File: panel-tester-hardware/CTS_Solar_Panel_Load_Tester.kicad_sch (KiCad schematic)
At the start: 11 parts, among them J1 Screw_Terminal_01x02, J2 Conn_01x02_Pin, J3 Conn_01x07, U1 INA219AxD, U2 LM311PW

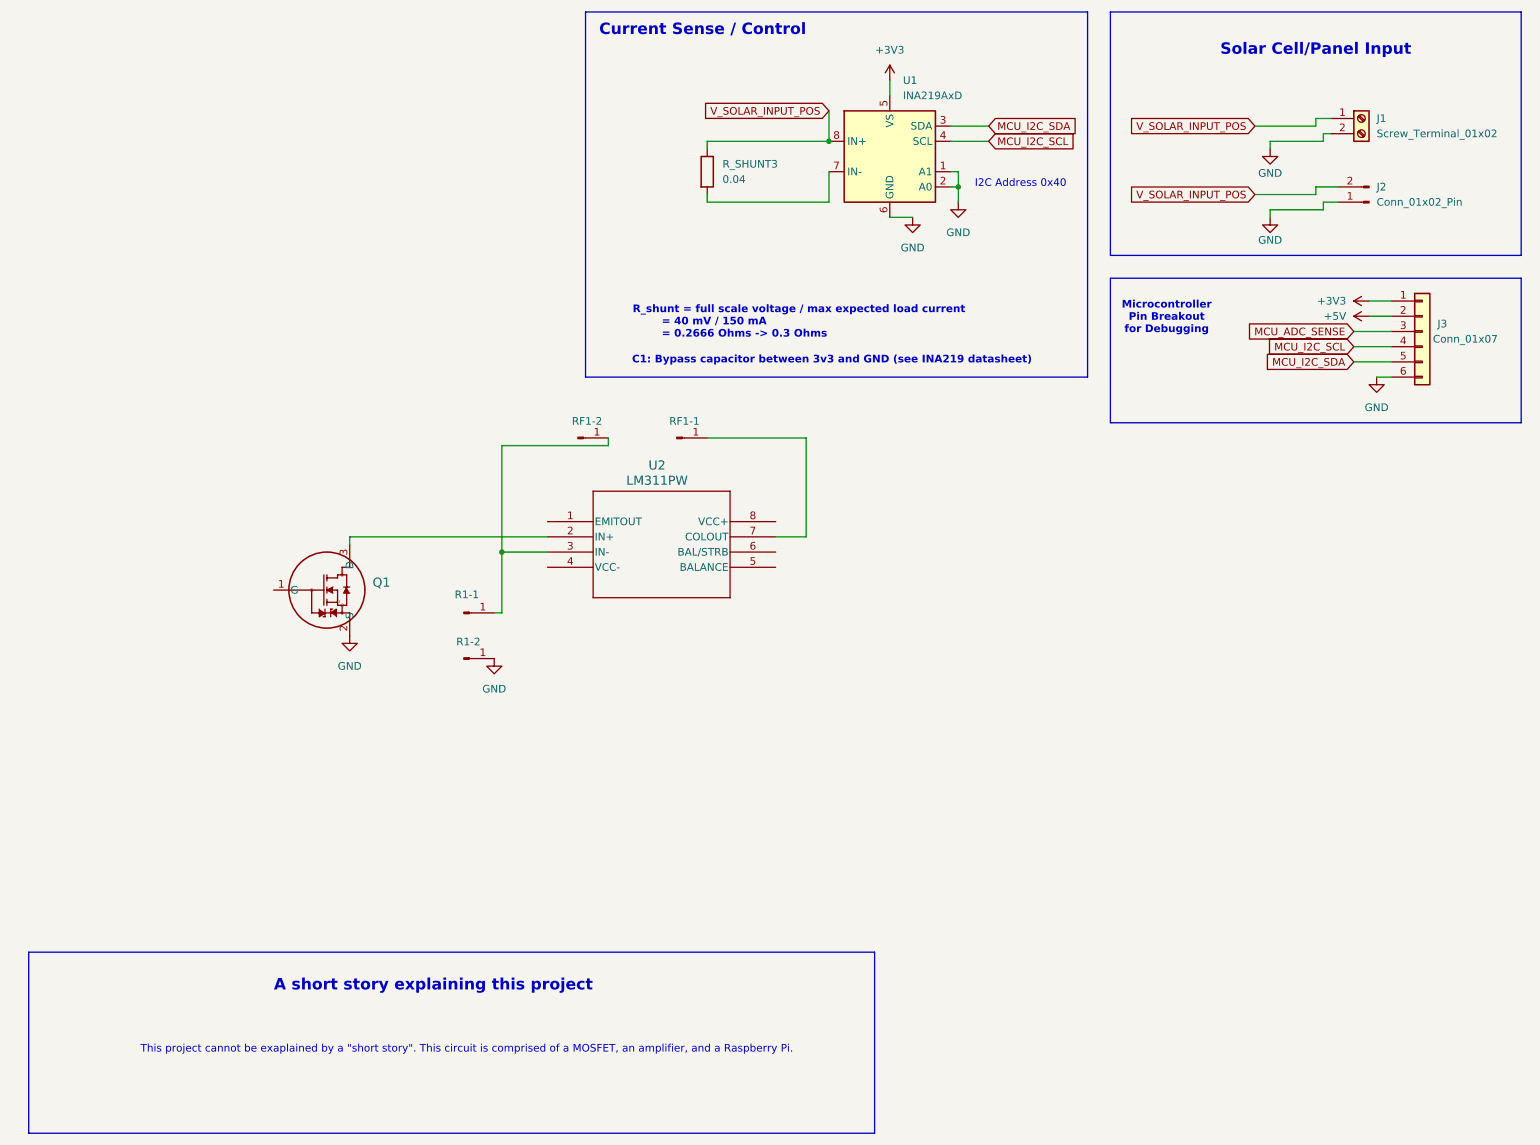
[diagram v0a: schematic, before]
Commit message: fixed footprints and added headers
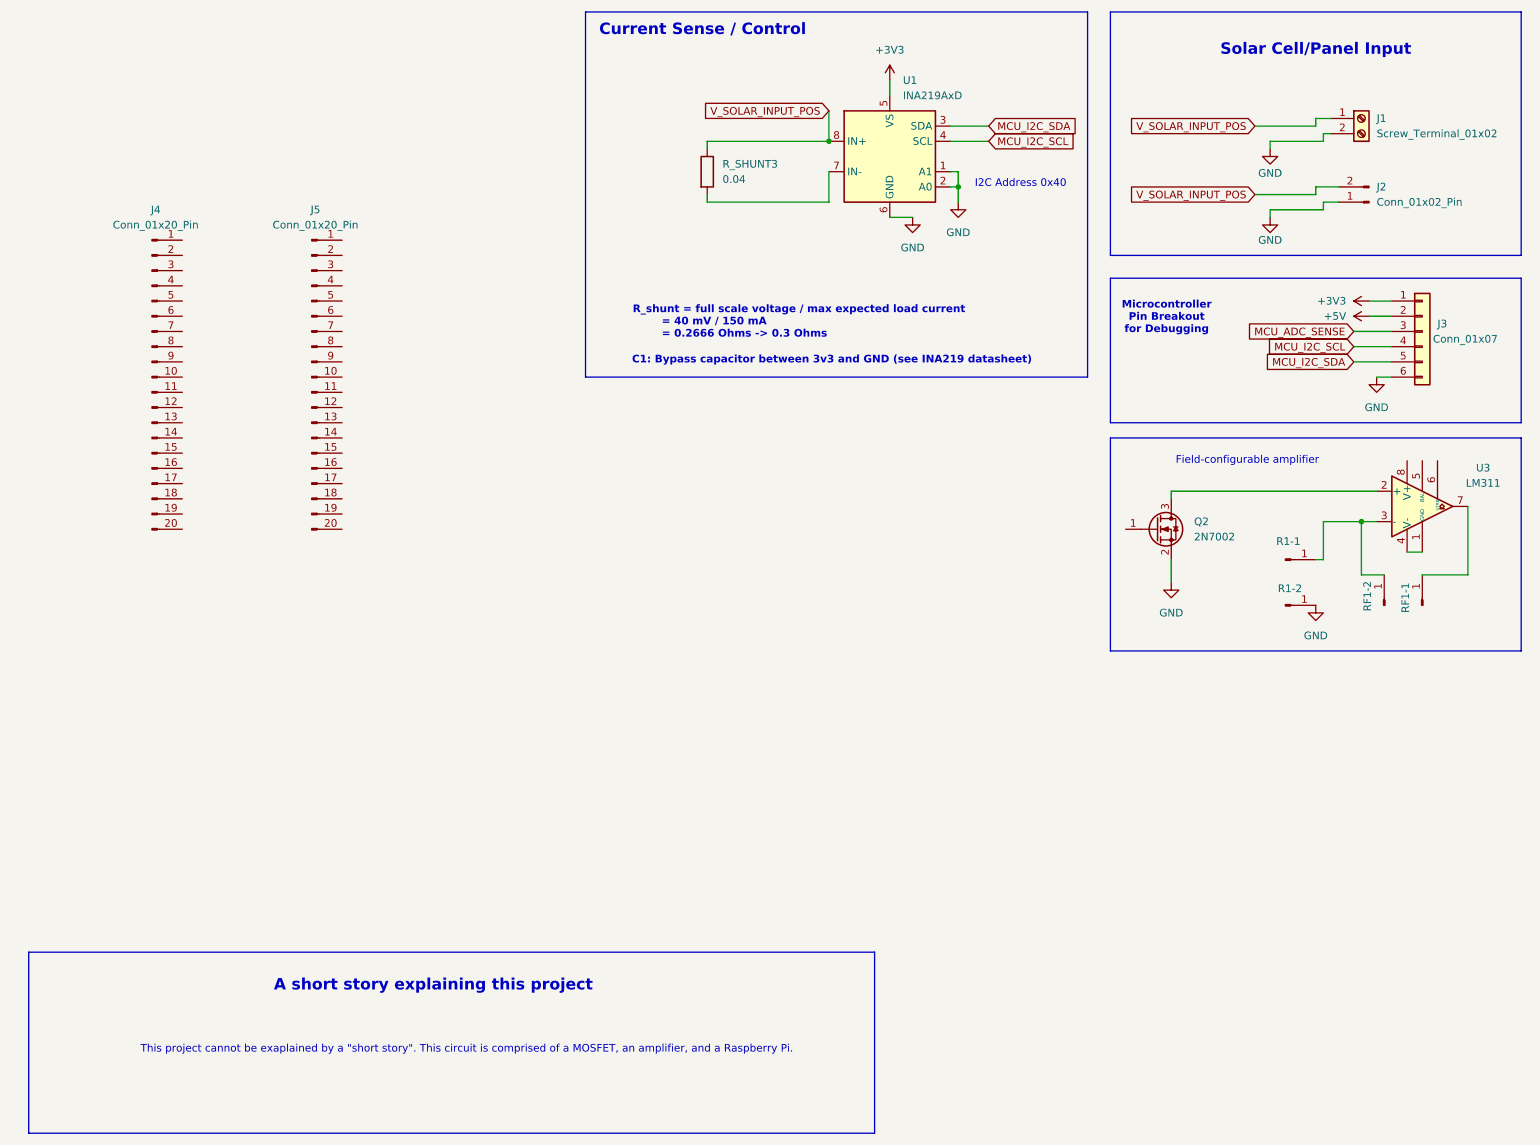
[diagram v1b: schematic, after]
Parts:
- removed Q1: ~, mosfet:TO-236AB_SOT23_NEX, symbol mosfet:2N7002NXAKR
- removed U2: LM311PW, PW8, symbol lm311opamp:LM311PW
- added J4, J5: Conn_01x20_Pin, Connector_PinHeader_2.54mm:PinHeader_1x20_P2.54mm_Vertical, symbol Connector:Conn_01x20_Pin
- added Q2: 2N7002, Package_TO_SOT_SMD:SOT-23, symbol Transistor_FET:2N7002
- added U3: LM311, Package_SO:SOIC-8-1EP_3.9x4.9mm_P1.27mm_EP2.95x4.9mm_Mask2.71x3.4mm, symbol Comparator:LM311
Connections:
- net GND: now also Q2.2 (S)
- net at R1-1.1 (Pin_1), RF1-2.1 (Pin_1): now also U3.3 (-)
- net at RF1-1.1 (Pin_1): now also U3.7
- new net: Q2.3 (D), U3.2 (+)
- new net: U3.1 (GND), U3.4 (V-)
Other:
- note added: "Field-configurable amplifier"
- moved on the sheet: R1-1, R1-2, RF1-1, RF1-2

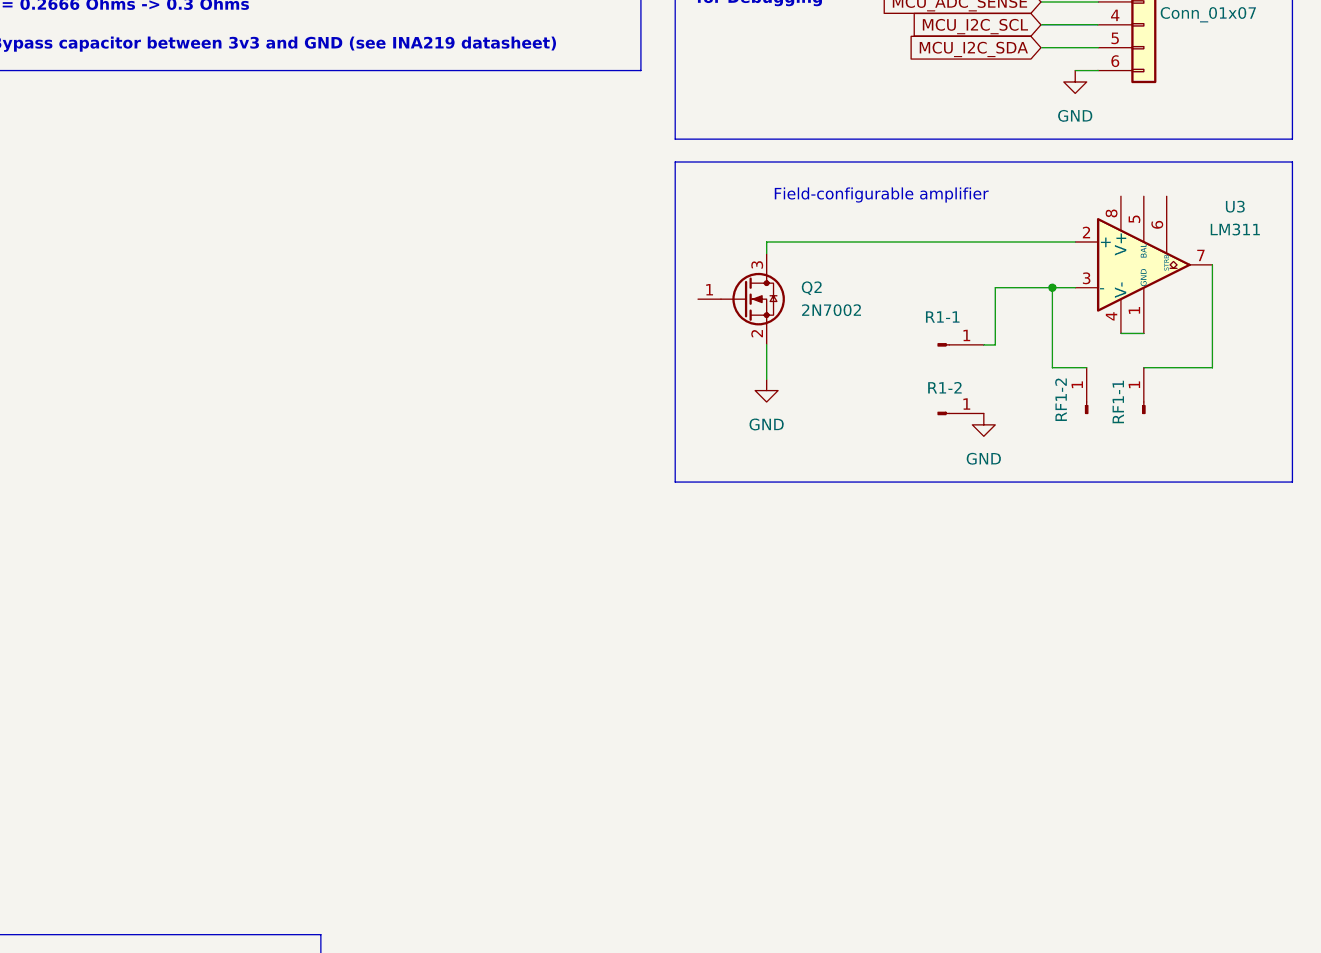
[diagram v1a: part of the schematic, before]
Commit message: added DAC
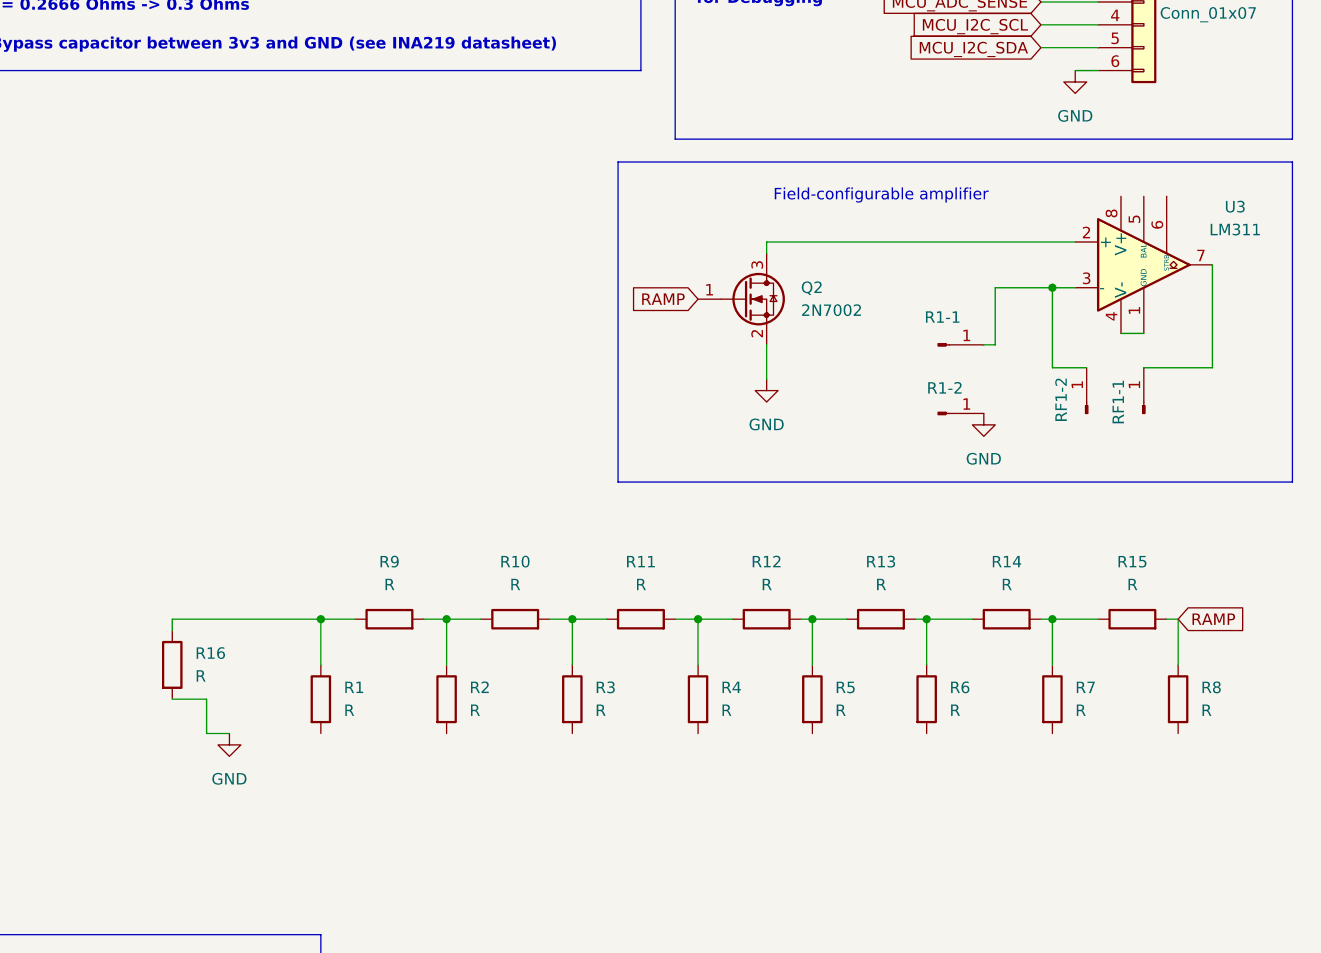
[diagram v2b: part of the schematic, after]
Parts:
- added R1, R10, R11, R12, R13, R14, R15, R16, R2, R3, R4, R5, R6, R7, R8, R9: R, symbol Device:R
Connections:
- net GND: now also R16.2
- net RAMP: now reaches Q2.1 (G)
- net RAMP: now also R15.2, R8.1
- new net: R13.2, R14.1, R6.1
- new net: R14.2, R15.1, R7.1
- new net: R10.2, R11.1, R3.1
- new net: R10.1, R2.1, R9.2
- new net: R1.1, R16.1, R9.1
- new net: R12.2, R13.1, R5.1
- new net: R11.2, R12.1, R4.1

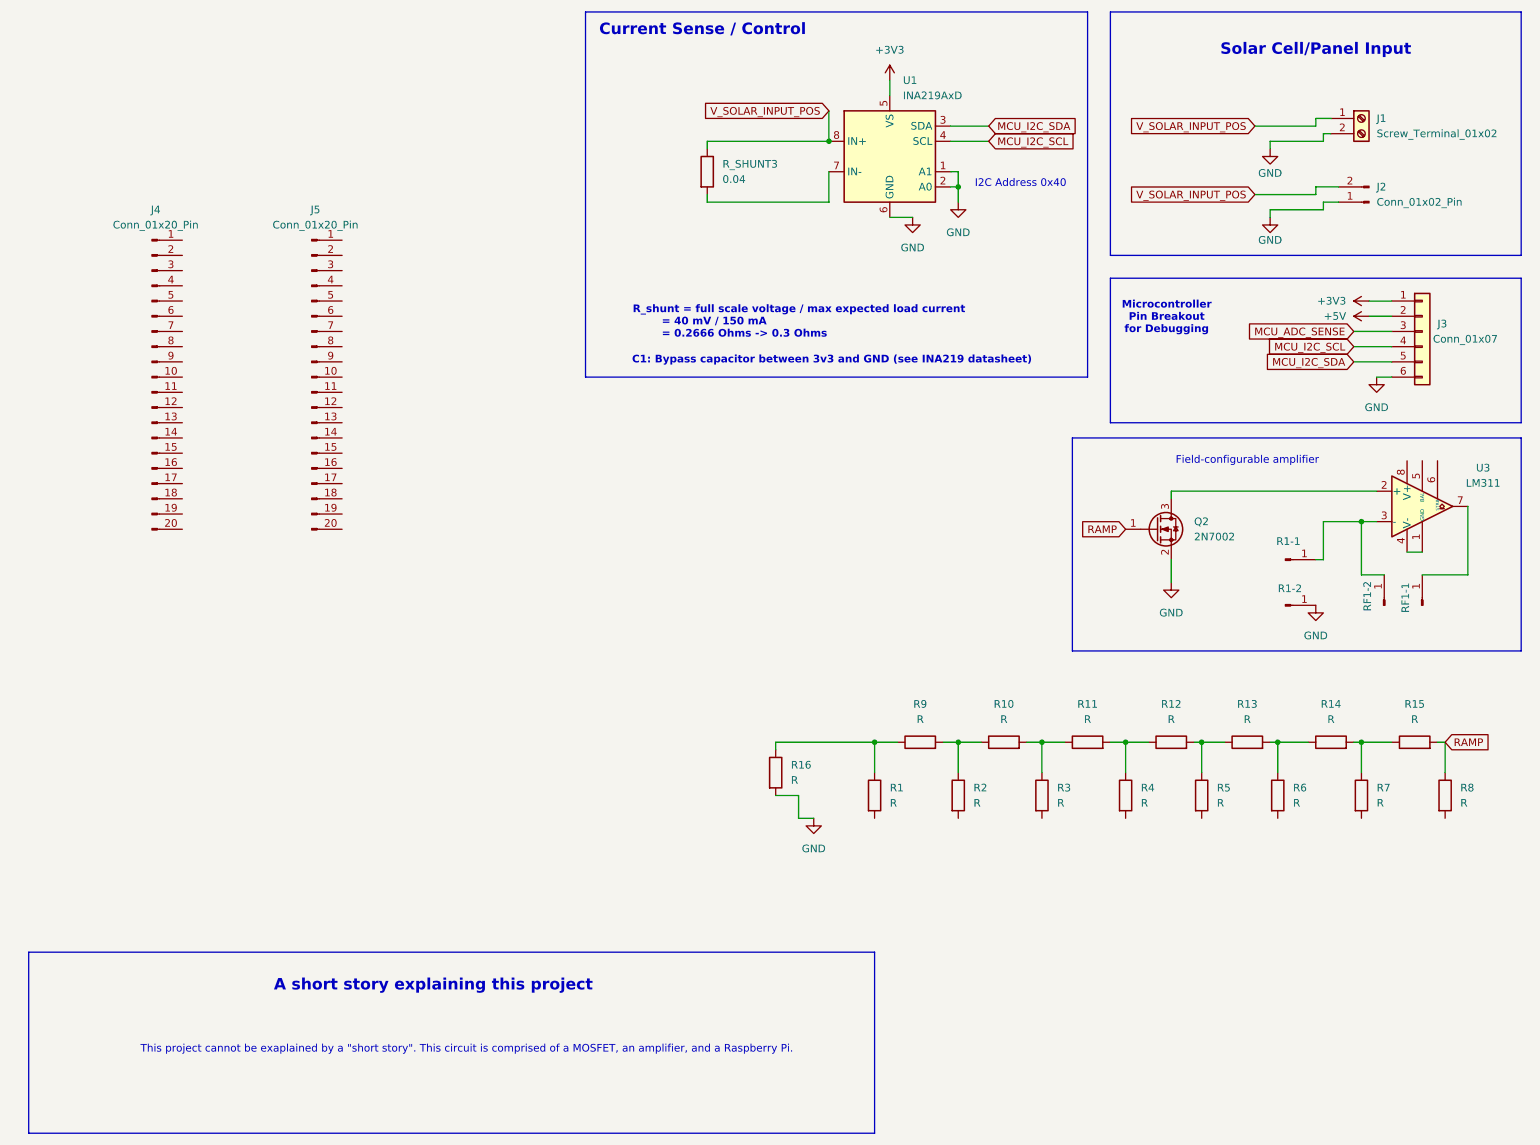
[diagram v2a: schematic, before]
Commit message: PCB passes DRC
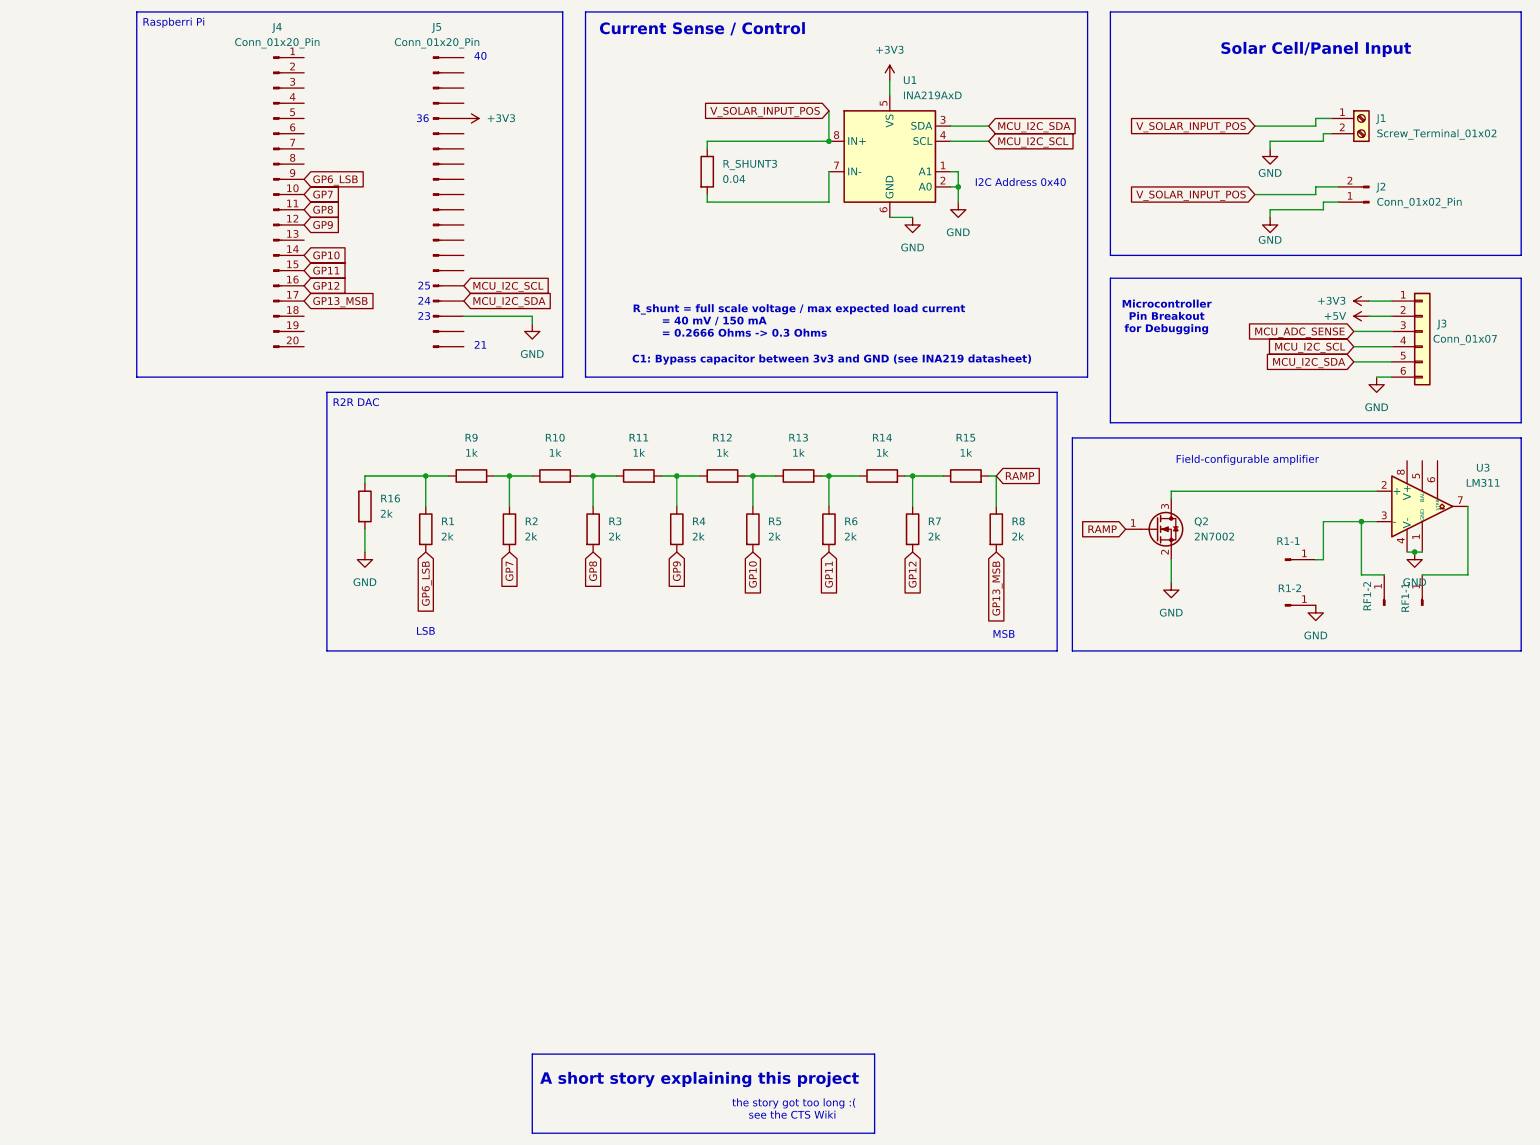
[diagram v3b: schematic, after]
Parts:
- R1, R16, R2, R3, R4, R5, R6, R7, R8: value R -> 2k; footprint (none) -> Resistor_SMD:R_1206_3216Metric_Pad1.30x1.75mm_HandSolder
- R10, R11, R12, R13, R14, R15, R9: value R -> 1k; footprint (none) -> Resistor_SMD:R_1206_3216Metric_Pad1.30x1.75mm_HandSolder
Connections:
- net +3V3: now also J5.5 (Pin_5)
- net GND: now also J5.18 (Pin_18), U3.1 (GND), U3.4 (V-)
- net MCU_I2C_SCL: now also J5.16 (Pin_16)
- net MCU_I2C_SDA: now also J5.17 (Pin_17)
- net GP11: now reaches R6.2
- net GP11: now also J4.15 (Pin_15)
- net GP12: now reaches R7.2
- net GP12: now also J4.16 (Pin_16)
- net GP8: now reaches R3.2
- net GP8: now also J4.11 (Pin_11)
- net GP13_MSB: now reaches R8.2
- net GP13_MSB: now also J4.17 (Pin_17)
- net GP7: now reaches R2.2
- net GP7: now also J4.10 (Pin_10)
- net GP6_LSB: now reaches R1.2
- net GP6_LSB: now also J4.9 (Pin_9)
- net GP10: now reaches R5.2
- net GP10: now also J4.14 (Pin_14)
- net GP9: now reaches R4.2
- net GP9: now also J4.12 (Pin_12)
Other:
- note added: "21"
- note added: "23"
- note added: "24"
- note added: "25"
- note added: "36"
- note added: "40"
- note added: "LSB"
- note added: "MSB"
- note added: "the story got too long :( see the CTS Wiki"
- note removed: "This project cannot be exaplained by a {dblquote}short story{dblquote}. This circuit is comprised of a MOSFET, an amplifier, and a Raspberry Pi."
- moved on the sheet: J4, R1, R10, R11, R12, R13, R14, R15, R16, R2, R3, R4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

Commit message: checklist almost done
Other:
- company: (none) -> CalgaryToSpace
- title: (none) -> Solar Panel Load Tester
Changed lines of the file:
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@@
 	(generator_version "9.0")
 	(paper "USLetter")
+	(title_block
+		(title "Solar Panel Load Tester")
+		(date "2026-01-17")
+		(rev "3")
+		(company "CalgaryToSpace")
+	)
 	(rectangle
 		(start 107.95 15.24)
